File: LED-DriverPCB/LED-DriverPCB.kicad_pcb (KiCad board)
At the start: 4 copper layers, 44 parts, among them J1 Screw_Terminal_01x03, J12 Screw_Terminal_01x02, J13 Screw_Terminal_01x02, J14 Screw_Terminal_01x02, J15 Screw_Terminal_01x02, J16 Screw_Terminal_01x02, J17 Screw_Terminal_01x02, J18 Screw_Terminal_01x02, J19 Screw_Terminal_01x02, J2 Screw_Terminal_01x03, J20 Conn_ARM_SWD_TagConnect_TC2030, J3 Screw_Terminal_01x03, J4 Screw_Terminal_01x03, J5 Screw_Terminal_01x03, J6 Screw_Terminal_01x03, J7 Screw_Terminal_01x03, J8 Screw_Terminal_01x03, J9 USB_C_Receptacle_USB2.0_16P, SW1 SW_SPDT, U1 STM32F103RCTx, U2 TXB0108PW, U3 AMS1117-3.3, U4 USBLC6-2SC6, X1 8MHz

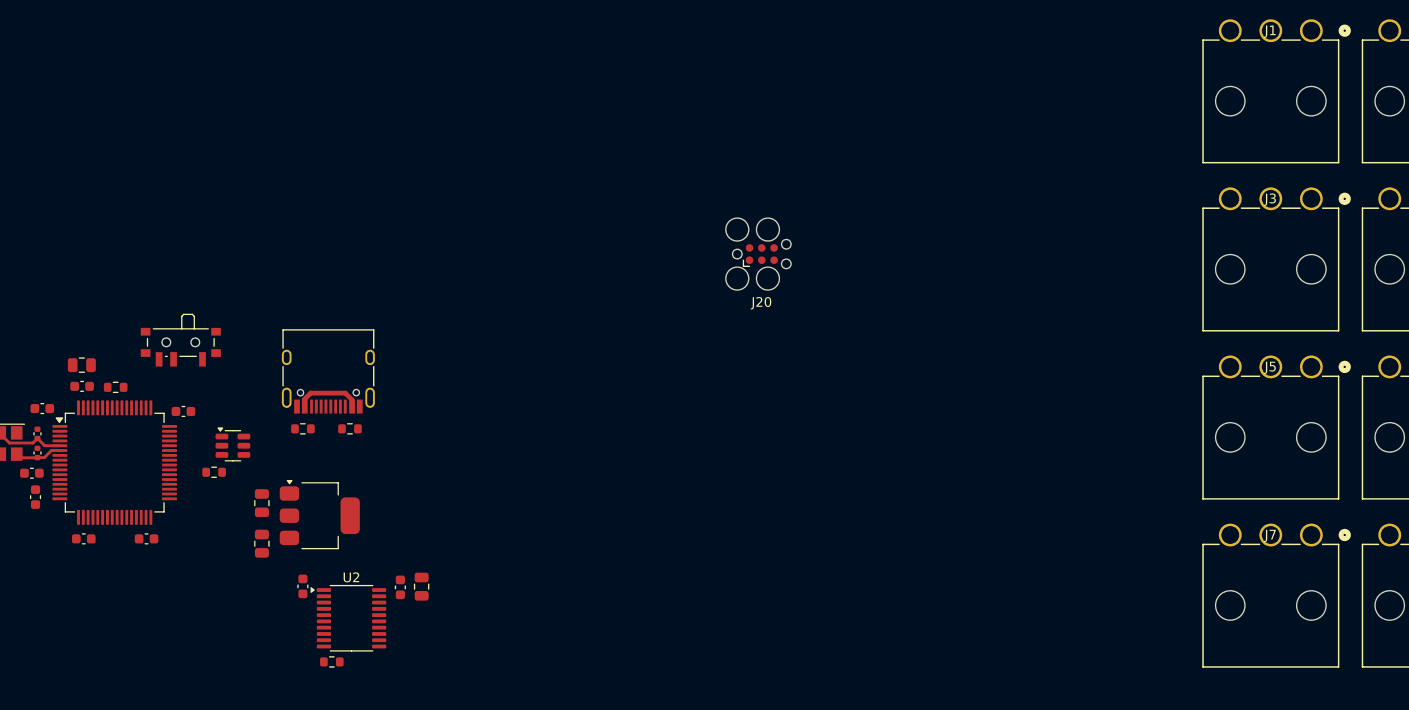
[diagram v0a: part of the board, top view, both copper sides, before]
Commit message: Rough layout completed
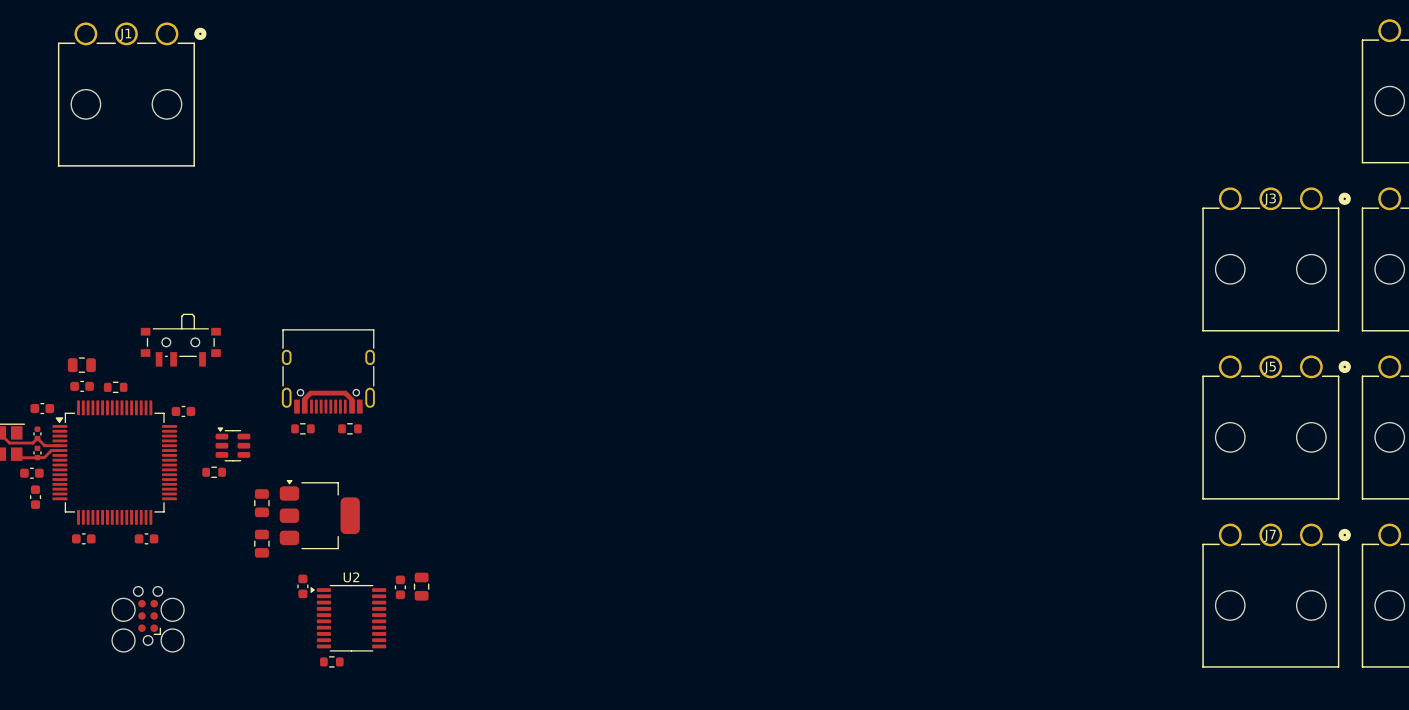
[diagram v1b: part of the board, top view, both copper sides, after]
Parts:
- moved J1 118.6 mm to (82.9, 67.1)
- moved J20 73.8 mm to (81.0, 127.4), turned to 90 degrees
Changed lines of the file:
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@@
 	(footprint "Connector:Tag-Connect_TC2030-IDC-FP_2x03_P1.27mm_Vertical"
 		(layer "F.Cu")
-		(at 144.5445 89.89345)
+		(at 80.96 127.385 90)
 		(descr "Tag-Connect programming header; http://www.tag-connect.com/Materials/TC2030-IDC.pdf")
 		(tags "tag connect programming header pogo pins")
 		(property "Reference" "J20"
-			(at 0 5 0)
-			(layer "F.SilkS")
+			(at 0 5 90)
+			(layer "F.Fab")
 			(effects
 				(font
@@
 		)
 		(property "Value" "Conn_ARM_SWD_TagConnect_TC2030"
-			(at 0 -4.7 0)
+			(at 0 -4.7 90)
 			(layer "F.Fab")
 			(effects
@@
 		)
 		(property "Datasheet" "https://www.tag-connect.com/wp-content/uploads/bsk-pdf-manager/TC2030-CTX_1.pdf"
-			(at 0 0 0)
+			(at 0 0 90)
 			(unlocked yes)
 			(layer "F.Fab")
@@
 		)
 		(property "Description" "Tag-Connect ARM Cortex SWD JTAG connector, 6 pin"
-			(at 0 0 0)
+			(at 0 0 90)
 			(unlocked yes)
 			(layer "F.Fab")
@@
 		(attr exclude_from_pos_files exclude_from_bom)
 		(fp_line
-			(start -1.905 1.27)
-			(end -1.905 0.635)
+			(start -1.27 1.27)
+			(end -1.905 1.27)
 			(stroke
 				(width 0.12)
@@
 		)
 		(fp_line
-			(start -1.27 1.27)
-			(end -1.905 1.27)
+			(start -1.905 1.27)
+			(end -1.905 0.635)
 			(stroke
 				(width 0.12)
@@
 		)
 		(fp_line
-			(start -4.25 -4.25)
-			(end 3.75 -4.25)
+			(start 3.75 -4.25)
+			(end 3.75 4.25)
 			(stroke
 				(width 0.05)
@@
 		)
 		(fp_line
-			(start -4.25 4.25)
-			(end -4.25 -4.25)
+			(start -4.25 -4.25)
+			(end 3.75 -4.25)
 			(stroke
 				(width 0.05)
@@
 		)
 		(fp_line
-			(start 3.75 -4.25)
-			(end 3.75 4.25)
+			(start 3.75 4.25)
+			(end -4.25 4.25)
 			(stroke
 				(width 0.05)
@@
 		)
 		(fp_line
-			(start 3.75 4.25)
-			(end -4.25 4.25)
+			(start -4.25 4.25)
+			(end -4.25 -4.25)
 			(stroke
 				(width 0.05)
@@
 		)
 		(fp_text user "KEEPOUT"
-			(at 0 0 0)
+			(at 0 0 90)
 			(layer "Cmts.User")
 			(effects
@@
 		)
 		(fp_text user "${REFERENCE}"
-			(at 0 0 0)
+			(at 0 0 90)
 			(layer "F.Fab")
 			(effects
@@
 		)
 		(pad "" np_thru_hole circle
-			(at -2.54 -2.54)
+			(at -2.54 -2.54 90)
 			(size 2.3749 2.3749)
 			(drill 2.3749)
@@
 		)
 		(pad "" np_thru_hole circle
-			(at -2.54 0)
+			(at -2.54 0 90)
 			(size 0.9906 0.9906)
 			(drill 0.9906)
@@
 		)
 		(pad "" np_thru_hole circle
-			(at -2.54 2.54)
+			(at -2.54 2.54 90)
 			(size 2.3749 2.3749)
 			(drill 2.3749)
@@
 		)
 		(pad "" np_thru_hole circle
-			(at 0.635 -2.54)
+			(at 0.635 -2.54 90)
 			(size 2.3749 2.3749)
 			(drill 2.3749)
@@
 		)
 		(pad "" np_thru_hole circle
-			(at 0.635 2.54)
+			(at 0.635 2.54 90)
 			(size 2.3749 2.3749)
 			(drill 2.3749)
@@
 		)
 		(pad "" np_thru_hole circle
-			(at 2.54 -1.016)
+			(at 2.54 -1.016 90)
 			(size 0.9906 0.9906)
 			(drill 0.9906)
@@
 		)
 		(pad "" np_thru_hole circle
-			(at 2.54 1.016)
+			(at 2.54 1.016 90)
 			(size 0.9906 0.9906)
 			(drill 0.9906)
@@
 		)
 		(pad "1" connect circle
-			(at -1.27 0.635)
+			(at -1.27 0.635 90)
 			(size 0.7874 0.7874)
 			(layers "F.Cu" "F.Mask")
@@
 		)
 		(pad "2" connect circle
-			(at -1.27 -0.635)
+			(at -1.27 -0.635 90)
 			(size 0.7874 0.7874)
 			(layers "F.Cu" "F.Mask")
@@
 		)
 		(pad "3" connect circle
-			(at 0 0.635)
+			(at 0 0.635 90)
 			(size 0.7874 0.7874)
 			(layers "F.Cu" "F.Mask")
@@
 		)
 		(pad "4" connect circle
-			(at 0 -0.635)
+			(at 0 -0.635 90)
 			(size 0.7874 0.7874)
 			(layers "F.Cu" "F.Mask")
@@
 		)
 		(pad "5" connect circle
-			(at 1.27 0.635)
+			(at 1.27 0.635 90)
 			(size 0.7874 0.7874)
 			(layers "F.Cu" "F.Mask")
@@
 		)
 		(pad "6" connect circle
-			(at 1.27 -0.635)
+			(at 1.27 -0.635 90)
 			(size 0.7874 0.7874)
 			(layers "F.Cu" "F.Mask")
@@
 			(polygon
 				(pts
-					(xy 145.8145 89.25845) (xy 143.2745 89.25845) (xy 143.2745 90.52845) (xy 145.8145 90.52845)
+					(xy 80.325 126.115) (xy 80.325 128.655) (xy 81.595 128.655) (xy 81.595 126.115)
 				)
 			)
@@
 	(footprint "39303037:CONN_5569-03A4&slash_5_MOL"
 		(layer "F.Cu")
-		(at 201.4806 66.751397)
+		(at 82.916599 67.0819)
 		(tags "39303037 ")
 		(property "Reference" "J1"

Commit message: Finished edge cuts
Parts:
- added H1: MountingHole, MountingHole:MountingHole_3.2mm_M3, F.Cu at (120.5, 86.0)
- added H2: MountingHole, MountingHole:MountingHole_3.2mm_M3, F.Cu at (218.9, 86.0)
- added H3: MountingHole, MountingHole:MountingHole_3.2mm_M3, F.Cu at (238.1, 86.0)
- added H4: MountingHole, MountingHole:MountingHole_3.2mm_M3, F.Cu at (336.5, 86.0)
- added H5: MountingHole, MountingHole:MountingHole_3.2mm_M3, F.Cu at (120.5, 200.3)
- added H6: MountingHole, MountingHole:MountingHole_3.2mm_M3, F.Cu at (218.9, 200.3)
- added H7: MountingHole, MountingHole:MountingHole_3.2mm_M3, F.Cu at (238.1, 200.3)
- added H8: MountingHole, MountingHole:MountingHole_3.2mm_M3, F.Cu at (336.5, 200.3)
- moved J12 233.7 mm to (41.9, 376.8)
- moved J13 233.7 mm to (61.9, 376.8)
- moved J14 233.7 mm to (81.9, 376.8)
- moved J15 233.7 mm to (101.9, 376.9)
- moved J16 233.7 mm to (122.0, 376.9)
- moved J17 233.7 mm to (142.0, 376.9)
- moved J18 222.4 mm to (30.3, 299.0)
- moved J19 222.4 mm to (50.2, 299.1)
- moved J2 222.4 mm to (57.5, 220.8)
- moved J3 222.4 mm to (41.0, 238.2)
- moved J4 222.4 mm to (57.5, 238.2)
- moved J5 222.4 mm to (41.0, 255.6)
- moved J6 222.4 mm to (57.5, 255.6)
- moved J7 222.4 mm to (41.0, 273.0)
- moved J8 222.4 mm to (57.5, 273.0)
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
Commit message: Placed parts
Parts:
- moved J8 277.6 mm to (326.2, 203.3)
- moved J9 276.2 mm to (348.0, 138.0), turned to 90 degrees
- moved U4 274.3 mm to (337.0, 138.0)
- moved J7 272.3 mm to (304.2, 203.3)
- moved R3 271.7 mm to (341.7, 135.4), turned to -90 degrees
- moved R2 267.3 mm to (341.7, 140.2), turned to 90 degrees
- moved J12 261.5 mm to (117.6, 126.5), turned to -90 degrees
- moved J13 245.2 mm to (117.5, 138.0), turned to -90 degrees
- moved J6 229.7 mm to (281.2, 203.3)
- moved J14 227.1 mm to (117.6, 152.5), turned to -90 degrees
- moved J5 223.4 mm to (258.2, 203.3)
- moved J18 217.3 mm to (117.5, 100.0), turned to -90 degrees
- moved J15 212.0 mm to (117.6, 165.5), turned to -90 degrees
- moved J16 198.4 mm to (117.5, 178.5), turned to -90 degrees
- moved J19 196.5 mm to (117.5, 114.5), turned to -90 degrees
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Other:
- board outline added: 246 x 144.3 mm

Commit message: Small changes
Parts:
- removed SW1: SW_SPDT, Button_Switch_SMD:SW_SPDT_PCM12
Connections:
- net Net-(U2-OE) renamed /SHIFTER_OE
- R1 pad 1: /SW_BOOT -> GND

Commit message: Aligned connectors
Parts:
- moved J8 2.93 mm to (323.3, 203.0)
- moved J7 2.15 mm to (302.1, 203.0)
- moved J1 1.99 mm to (205.7, 203.0)
- moved J5 1.49 mm to (259.6, 203.0)
- moved J4 1.22 mm to (184.5, 203.0)
- moved J3 0.51 mm to (163.3, 203.0)
- moved J6 0.47 mm to (280.9, 203.0)
- moved J2 0.17 mm to (142.1, 203.0)
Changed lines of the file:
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@@
 	(footprint "39303037:CONN_5569-03A4&slash_5_MOL"
 		(layer "F.Cu")
-		(at 163.695599 203.3229)
+		(at 163.307099 203)
 		(tags "39303037 ")
 		(property "Reference" "J3"
@@
 	(footprint "39303037:CONN_5569-03A4&slash_5_MOL"
 		(layer "F.Cu")
-		(at 281.195599 203.3229)
+		(at 280.856599 203)
 		(tags "39303037 ")
 		(property "Reference" "J6"
@@
 	(footprint "39303037:CONN_5569-03A4&slash_5_MOL"
 		(layer "F.Cu")
-		(at 142.195599 203.1409)
+		(at 142.096099 203)
 		(tags "39303037 ")
 		(property "Reference" "J2"
@@
 	(footprint "39303037:CONN_5569-03A4&slash_5_MOL"
 		(layer "F.Cu")
-		(at 304.195599 203.3229)
+		(at 302.067599 203)
 		(tags "39303037 ")
 		(property "Reference" "J7"
@@
 	(footprint "39303037:CONN_5569-03A4&slash_5_MOL"
 		(layer "F.Cu")
-		(at 326.195599 203.3229)
+		(at 323.278599 203)
 		(tags "39303037 ")
 		(property "Reference" "J8"
@@
 	(footprint "39303037:CONN_5569-03A4&slash_5_MOL"
 		(layer "F.Cu")
-		(at 185.695599 203.3229)
+		(at 184.518099 203)
 		(tags "39303037 ")
 		(property "Reference" "J4"
@@
 	(footprint "39303037:CONN_5569-03A4&slash_5_MOL"
 		(layer "F.Cu")
-		(at 207.695599 203.3229)
+		(at 205.729099 203)
 		(tags "39303037 ")
 		(property "Reference" "J1"
@@
 	(footprint "39303037:CONN_5569-03A4&slash_5_MOL"
 		(layer "F.Cu")
-		(at 258.195599 203.3229)
+		(at 259.645599 203)
 		(tags "39303037 ")
 		(property "Reference" "J5"

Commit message: Started routing
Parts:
- moved J8 181.2 mm to (142.1, 203.0)
- moved J2 160.0 mm to (302.1, 203.0)
- moved J7 138.8 mm to (163.3, 203.0)
- moved J3 117.5 mm to (280.9, 203.0)
- moved J1 117.5 mm to (323.3, 203.0)
- moved J6 96.3 mm to (184.5, 203.0)
- moved J4 75.1 mm to (259.6, 203.0)
- moved J18 74.7 mm to (118.0, 174.7)
- moved J19 72.8 mm to (118.0, 187.3)
- moved J5 53.9 mm to (205.7, 203.0)
- moved J16 29.0 mm to (118.0, 149.5)
- moved J15 28.6 mm to (118.0, 136.8)
- moved J14 28.2 mm to (118.0, 124.2)
- moved J17 27.9 mm to (118.0, 162.1)
- moved J12 27.5 mm to (118.0, 99.0)
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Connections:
- U4 pad 1: /USB_STM_D- -> /USB_STM_D+
- U4 pad 3: /USB_STM_D+ -> /USB_STM_D-
- U4 pad 4: /USB_CON_D+ -> /USB_CON_D-
- U4 pad 6: /USB_CON_D- -> /USB_CON_D+
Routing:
- net /STR1_DATA: track 0.00 -> 131.1 mm
- net /STR8_DATA: track 0.00 -> 130.6 mm
- net /STR2_DATA: track 0.00 -> 110.8 mm
- net /STR7_DATA: track 0.00 -> 110.1 mm
- net /USB_STM_D-: track 0.00 -> 102.7 mm
- net /USB_STM_D+: track 0.00 -> 102.7 mm
- net /STR3_DATA: track 0.00 -> 90.2 mm
- net /STR6_DATA: track 0.00 -> 89.5 mm
- net /STR4_DATA: track 0.00 -> 69.4 mm
- net /STR5_DATA: track 0.00 -> 68.9 mm
- net /PWM_TIM5_CH1: track 0.00 -> 26.1 mm
- net /PWM_TIM5_CH2: track 0.00 -> 25.3 mm
- net /PWM_TIM5_CH3: track 0.00 -> 20.5 mm, vias 0 -> 2
- net /PWM_TIM5_CH4: track 0.00 -> 17.0 mm, vias 0 -> 2
- net GND: track 0.00 -> 16.6 mm, vias 0 -> 3
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
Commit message: More routing
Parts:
- moved R5 5.06 mm to (239.1, 135.5), turned to -90 degrees
- moved J20 2.17 mm to (234.8, 127.8), turned to 180 degrees
- moved C6 1.39 mm to (235.8, 135.5)
- moved C3 0.28 mm to (231.5, 147.2)
- moved C11 0.22 mm to (238.4, 152.0)
- moved C12 0.21 mm to (238.4, 147.9)
- moved R1 0.11 mm to (228.0, 131.7)
- moved C5 0.07 mm to (220.6, 133.9)
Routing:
- net /STR1_PWR: track 0.00 -> 300.6 mm
- net /STR2_PWR: track 0.00 -> 270.6 mm
- net /STR3_PWR: track 0.00 -> 240.6 mm
- net /STR4_PWR: track 0.00 -> 178.6 mm
- net VBUS: track 15.0 -> 162.4 mm
- net /STR5_PWR: track 0.00 -> 124.3 mm
- net +3.3V: track 9.58 -> 114.8 mm, vias 0 -> 10
- net /STR6_PWR: track 0.00 -> 100.1 mm
- net /STR7_PWR: track 0.00 -> 66.7 mm
- net /SWD_NRST: track 0.00 -> 38.2 mm, vias 0 -> 2
- net /STR8_PWR: track 0.00 -> 33.0 mm
- net GND: track 16.6 -> 40.0 mm, vias 3 -> 59
- net /SWD_DIO: track 0.00 -> 18.2 mm
- net /SWD_SWO: track 0.00 -> 10.6 mm
- net /SWD_CLK: track 0.00 -> 9.47 mm
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- added copper zone on F.Cu, net +3.3V
- added copper zone on In1.Cu, net GND
- added copper zone on In2.Cu, net GND

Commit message: Small changes
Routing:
- net GND: track 40.0 -> 49.7 mm, vias 59 -> 67
- net /SWD_NRST: track 38.2 -> 40.0 mm, vias 2 -> 4
- net VBUS: track 162.4 -> 162.1 mm, vias 1 -> 0
